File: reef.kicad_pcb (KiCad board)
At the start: 2 copper layers, 60 parts, among them J1 T4140012051-000, J2 T4140012051-000, U1 nice_nano

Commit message: PCB Layout
layout of keys, controller board, connectors + routed matrix columns
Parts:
- added MX1: MX-NoLED, MX_Only:MXOnly-1U-Hotswap, B.Cu at (46.8, 62.7)
- added MX10: MX-NoLED, MX_Only:MXOnly-1U-Hotswap, B.Cu at (84.9, 75.4)
- added MX11: MX-NoLED, MX_Only:MXOnly-1U-Hotswap, B.Cu at (84.9, 94.5)
- added MX12: MX-NoLED, MX_Only:MXOnly-1U-Hotswap, B.Cu at (84.9, 113.5)
- added MX13: MX-NoLED, MX_Only:MXOnly-1U-Hotswap, B.Cu at (104.0, 59.5)
- added MX14: MX-NoLED, MX_Only:MXOnly-1U-Hotswap, B.Cu at (104.0, 78.6)
- added MX15: MX-NoLED, MX_Only:MXOnly-1U-Hotswap, B.Cu at (104.0, 97.6)
- added MX16: MX-NoLED, MX_Only:MXOnly-1U-Hotswap, B.Cu at (104.0, 116.7)
- added MX17: MX-NoLED, MX_Only:MXOnly-1U-Hotswap, B.Cu at (123.0, 62.7)
- added MX18: MX-NoLED, MX_Only:MXOnly-1U-Hotswap, B.Cu at (123.0, 81.8)
- added MX19: MX-NoLED, MX_Only:MXOnly-1U-Hotswap, B.Cu at (123.0, 100.8)
- added MX2: MX-NoLED, MX_Only:MXOnly-1U-Hotswap, B.Cu at (46.8, 81.8)
- added MX20: MX-NoLED, MX_Only:MXOnly-1U-Hotswap, B.Cu at (123.0, 119.9)
- added MX21: MX-NoLED, MX_Only:MXOnly-1U-Hotswap, B.Cu at (142.1, 65.9)
- added MX22: MX-NoLED, MX_Only:MXOnly-1U-Hotswap, B.Cu at (142.1, 84.9)
- added MX23: MX-NoLED, MX_Only:MXOnly-1U-Hotswap, B.Cu at (142.1, 104.0)
- added MX24: MX-NoLED, MX_Only:MXOnly-1U-Hotswap, B.Cu at (217.5, 79.4)
- added MX25: MX-NoLED, MX_Only:MXOnly-2U-Hotswap, B.Cu at (217.5, 108.0)
- added MX26: MX-NoLED, MX_Only:MXOnly-1.25U-Hotswap, B.Cu at (238.9, 79.4)
- added MX27: MX-NoLED, MX_Only:MXOnly-1.25U-Hotswap, B.Cu at (238.9, 98.4)
- added MX28: MX-NoLED, MX_Only:MXOnly-1.25U-Hotswap, B.Cu at (238.9, 117.5)
- added MX3: MX-NoLED, MX_Only:MXOnly-1U-Hotswap, B.Cu at (46.8, 100.8)
- added MX4: MX-NoLED, MX_Only:MXOnly-1U-Hotswap, B.Cu at (46.8, 119.9)
- added MX5: MX-NoLED, MX_Only:MXOnly-1U-Hotswap, B.Cu at (65.9, 59.5)
- added MX6: MX-NoLED, MX_Only:MXOnly-1U-Hotswap, B.Cu at (65.9, 78.6)
- added MX7: MX-NoLED, MX_Only:MXOnly-1U-Hotswap, B.Cu at (65.9, 97.6)
- added MX8: MX-NoLED, MX_Only:MXOnly-1U-Hotswap, B.Cu at (65.9, 116.7)
- added MX9: MX-NoLED, MX_Only:MXOnly-1U-Hotswap, B.Cu at (84.9, 56.4)
- moved D26 231.1 mm to (260.4, 94.5)
- moved MX27 206.6 mm to (238.9, 98.4)
- moved D28 201.1 mm to (260.4, 107.2)
- moved MX25 193.4 mm to (217.5, 108.0), turned to 90 degrees
- moved D27 184.5 mm to (260.4, 100.8)
- moved MX28 182.2 mm to (238.9, 117.5)
- moved MX26 173.1 mm to (238.9, 79.4)
- moved D10 151.7 mm to (139.3, 164.5)
- moved D12 151.7 mm to (150.8, 161.1)
- moved D15 151.7 mm to (145.1, 161.1)
- moved D16 151.7 mm to (139.3, 171.2)
- moved D19 151.7 mm to (145.1, 164.5)
- moved D21 151.7 mm to (139.3, 161.1)
- moved D6 151.7 mm to (139.3, 167.8)
- moved J1 135.2 mm to (164.3, 70.8)
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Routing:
- net col_2: track 0.00 -> 143.6 mm, vias 0 -> 4
- net col_0: track 0.00 -> 143.6 mm, vias 0 -> 4
- net col_4: track 0.00 -> 143.6 mm, vias 0 -> 4
- net col_3: track 0.00 -> 143.6 mm, vias 0 -> 4
- net col_1: track 0.00 -> 143.6 mm, vias 0 -> 4
- net thc_7: track 0.00 -> 130.9 mm, vias 0 -> 3
- net thc_6: track 0.00 -> 111.9 mm, vias 0 -> 2
- net col_5: track 0.00 -> 102.9 mm, vias 0 -> 3

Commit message: PCB updates + importing keebio library
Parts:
- D1, D10, D11, D12, D13, D14, D15, D16, D17, D18, D19, D2, D20, D21, D22, D23, D24, D25, D26, D27, D28, D29, D3, D4, D5, D6, D7, D8, D9: footprint Diode_SMD:D_SOD-123 -> modified_footprints:D_SOD-123_reversible
- moved D24 43.0 mm to (217.5, 85.7)
- moved D25 40.5 mm to (224.6, 108.0), turned to 90 degrees
- moved D28 27.2 mm to (238.9, 123.8)
- moved D26 23.1 mm to (238.9, 85.7)
- moved D27 21.8 mm to (238.9, 104.8)

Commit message: Updated Layout
modified layout to use trrs to connect with thumb cluster, added connector for battery, and footprint for nice!view display
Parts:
- removed D29: D_Small, modified_footprints:D_SOD-123_reversible
- removed the MX24 at (217.5, 79.4) (x2)
- removed the MX25 at (217.5, 108.0) (x2)
- removed the MX26 at (238.9, 79.4) (x2)
- removed the MX27 at (238.9, 98.4) (x2)
- removed the MX28 at (238.9, 117.5) (x2)
- added MX24: MX-NoLED, MX_Only:MXOnly-1U-Hotswap, F.Cu at (142.1, 123.0)
- added MX25: MX-NoLED, MX_Only:MXOnly-2.25U-Hotswap, F.Cu at (337.3, 116.7)
- added MX26: MX-NoLED, MX_Only:MXOnly-1.5U-Hotswap, F.Cu at (361.2, 90.5)
- added MX27: MX-NoLED, MX_Only:MXOnly-1.5U-Hotswap, F.Cu at (361.2, 109.5)
- added MX28: MX-NoLED, MX_Only:MXOnly-1.5U-Hotswap, F.Cu at (361.2, 128.6)
- added U2: TRRS, Keebio-Parts:TRRS-PJ-320A, F.Cu at (166.7, 39.3)
- added U3: TRRS, Keebio-Parts:TRRS-PJ-320A, F.Cu at (329.8, 84.0)
- J1: value T4140012051-000 -> Conn_01x05_Female; footprint footprints:CONN5_T4140012051_TEC -> modified_footprints:nice_view_adapted
- J2: value T4140012051-000 -> Conn_01x02_Male; footprint footprints:CONN5_T4140012051_TEC -> Connector_JST:JST_PH_S2B-PH-K_1x02_P2.00mm_Horizontal
- moved D14 106.9 mm to (104.0, 84.9)
- moved D6 106.1 mm to (65.9, 91.3)
- moved D9 105.5 mm to (84.9, 69.1)
- moved D26 102.4 mm to (161.9, 153.2)
- moved D23 101.8 mm to (142.1, 110.3)
- moved D13 100.8 mm to (104.0, 65.9)
- moved D17 95.0 mm to (123.0, 69.1)
- moved D3 93.9 mm to (46.8, 113.5)
- moved D10 93.8 mm to (84.9, 88.1)
- moved D5 93.7 mm to (65.9, 72.2)
- moved D21 88.9 mm to (142.1, 72.2)
- moved D24 87.1 mm to (142.1, 129.4)
- moved D18 86.4 mm to (123.0, 88.1)
- moved D1 84.8 mm to (46.8, 75.4)
- moved D22 78.8 mm to (142.1, 91.3)
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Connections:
- D24 pad 1: thr_0 -> row_3
- D25 pad 1: thr_1 -> thr_0
- D28 pad 1: thr_2 -> thr_1
- J1 pad 1: row_2 -> mosi
- J1 pad 2: row_1 -> sck
- J1 pad 3: row_0 -> vcc
- J1 pad 4: col_6 -> gnd
- J1 pad 5: col_7 -> cs
- J2 pad 1: thr_2 -> bat+
- J2 pad 2: thr_1 -> gnd
- U1 pad 1: unconnected-(U1-Pad1) -> cs
- U1 pad 21: unconnected-(U1-Pad21) -> vcc
- U1 pad 23: unconnected-(U1-Pad23) -> gnd
- U1 pad 24: unconnected-(U1-Pad24) -> bat+
- U1 pad 3: unconnected-(U1-Pad3) -> gnd
- U1 pad 4: unconnected-(U1-Pad4) -> gnd
- U1 pad 5: unconnected-(U1-Pad5) -> mosi
- U1 pad 6: unconnected-(U1-Pad6) -> sck
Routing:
- net thc_7: track 130.9 -> 2.82 mm, vias 3 -> 0
- net thc_6: track 111.9 -> 6.38 mm, vias 2 -> 0
- net bat+: track 0.00 -> 9.48 mm
- net row_1: track 0.00 -> 6.82 mm
- net row_0: track 0.00 -> 6.63 mm
- net col_6: track 0.00 -> 6.63 mm
- net thr_1: track 0.00 -> 6.56 mm
- net thr_0: track 0.00 -> 6.38 mm
- net col_7: track 0.00 -> 2.57 mm
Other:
- board text added: "J2"

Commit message: Flipside Linkage
connected diode pads to their flipside counterparts, thumb cluster should now be fully routed, to be ground-planed later
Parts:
- D26: moved to B.Cu
- moved U3 108.4 mm to (221.9, 93.6)
- moved MX26 108.3 mm to (253.2, 99.2)
- moved MX27 108.3 mm to (253.2, 118.3)
- moved MX25 108.3 mm to (229.4, 125.4)
- moved MX28 108.3 mm to (253.2, 137.3)
- moved D26 102.9 mm to (253.2, 105.6), turned to 180 degrees
- moved D28 86.0 mm to (253.2, 143.7)
- moved D27 79.3 mm to (253.2, 124.6)
- moved D25 57.9 mm to (235.7, 125.4), turned to 90 degrees
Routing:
- net thc_6: track 6.38 -> 91.3 mm, vias 0 -> 2
- net thc_7: track 2.82 -> 78.5 mm, vias 0 -> 2
- net thr_0: track 6.38 -> 69.8 mm, vias 0 -> 2
- net thr_1: track 6.56 -> 57.3 mm, vias 0 -> 2
- net row_3: track 0.00 -> 23.7 mm, vias 0 -> 6
- net row_1: track 6.82 -> 30.6 mm, vias 0 -> 6
- net row_2: track 0.00 -> 23.7 mm, vias 0 -> 6
- net row_0: track 6.63 -> 30.4 mm, vias 0 -> 6
- net mosi: track 0.00 -> 16.0 mm
- net sck: track 0.00 -> 15.0 mm
- net cs: track 0.00 -> 13.1 mm
- net gnd: track 0.00 -> 5.81 mm
- net Net-(D8-Pad2): track 0.00 -> 3.96 mm, vias 0 -> 1
- net Net-(D28-Pad2): track 0.00 -> 3.96 mm, vias 0 -> 1
- net Net-(D20-Pad2): track 0.00 -> 3.96 mm, vias 0 -> 1
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
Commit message: Thumb Cluster Routing
thumb cluster routing should NOW be complete (rows were not connected up previously)
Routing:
- net thr_1: track 57.3 -> 76.7 mm
- net Net-(D28-Pad2): track 3.96 -> 20.5 mm
- net Net-(D25-Pad2): track 3.30 -> 18.9 mm
- net Net-(D26-Pad2): track 3.96 -> 18.8 mm
- net Net-(D27-Pad2): track 3.89 -> 18.1 mm
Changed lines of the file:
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@@
   (segment (start 235.74375 123.7625) (end 235.74375 122.2375) (width 0.25) (layer "B.Cu") (net 28))
   (segment (start 235.74375 122.2375) (end 234.15625 120.65) (width 0.25) (layer "B.Cu") (net 28))
+  (segment (start 253.20625 125.4125) (end 253.20625 133.969296) (width 0.25) (layer "F.Cu") (net 29))
+  (segment (start 250.825 136.350546) (end 250.825 140.49375) (width 0.25) (layer "F.Cu") (net 29))
+  (segment (start 250.825 140.49375) (end 253.20625 142.875) (width 0.25) (layer "F.Cu") (net 29))
   (segment (start 253.20625 142.875) (end 252.35 142.875) (width 0.25) (layer "F.Cu") (net 29))
+  (segment (start 253.20625 133.969296) (end 250.825 136.350546) (width 0.25) (layer "F.Cu") (net 29))
   (segment (start 252.35 125.4125) (end 251.55625 124.61875) (width 0.25) (layer "F.Cu") (net 29))
   (segment (start 253.20625 125.4125) (end 252.35 125.4125) (width 0.25) (layer "F.Cu") (net 29))
@@
   (via (at 235.74375 125.4125) (size 0.8) (drill 0.4) (layers "F.Cu" "B.Cu") (net 30))
   (segment (start 235.74375 127.0625) (end 235.74375 125.4125) (width 0.25) (layer "B.Cu") (net 30))
+  (segment (start 231.795479 119.082979) (end 233.3625 120.65) (width 0.25) (layer "B.Cu") (net 30))
+  (segment (start 224.801271 119.082979) (end 231.795479 119.082979) (width 0.25) (layer "B.Cu") (net 30))
+  (segment (start 233.3625 123.03125) (end 235.74375 125.4125) (width 0.25) (layer "B.Cu") (net 30))
+  (segment (start 224.31375 119.5705) (end 224.801271 119.082979) (width 0.25) (layer "B.Cu") (net 30))
+  (segment (start 233.3625 120.65) (end 233.3625 123.03125) (width 0.25) (layer "B.Cu") (net 30))
+  (segment (start 246.876729 94.626271) (end 246.876729 100.826729) (width 0.25) (layer "F.Cu") (net 31))
+  (segment (start 247.36425 94.13875) (end 246.876729 94.626271) (width 0.25) (layer "F.Cu") (net 31))
   (segment (start 254.85625 105.56875) (end 254 105.56875) (width 0.25) (layer "F.Cu") (net 31))
+  (segment (start 249.2375 103.1875) (end 251.61875 103.1875) (width 0.25) (layer "F.Cu") (net 31))
+  (segment (start 246.876729 100.826729) (end 249.2375 103.1875) (width 0.25) (layer "F.Cu") (net 31))
+  (segment (start 251.61875 103.1875) (end 253.20625 104.775) (width 0.25) (layer "F.Cu") (net 31))
   (segment (start 254 105.56875) (end 253.20625 104.775) (width 0.25) (layer "F.Cu") (net 31))
   (via (at 253.20625 104.775) (size 0.8) (drill 0.4) (layers "F.Cu" "B.Cu") (net 31))
   (segment (start 252.35 104.775) (end 251.55625 105.56875) (width 0.25) (layer "B.Cu") (net 31))
   (segment (start 253.20625 104.775) (end 252.35 104.775) (width 0.25) (layer "B.Cu") (net 31))
+  (segment (start 247.36425 113.18875) (end 246.876729 113.676271) (width 0.25) (layer "F.Cu") (net 32))
   (segment (start 254.85625 124.61875) (end 253.831652 124.61875) (width 0.25) (layer "F.Cu") (net 32))
+  (segment (start 246.876729 113.676271) (end 246.876729 118.78632) (width 0.25) (layer "F.Cu") (net 32))
+  (segment (start 251.121659 123.03125) (end 252.244152 123.03125) (width 0.25) (layer "F.Cu") (net 32))
   (segment (start 253.831652 124.61875) (end 253.122076 123.909174) (width 0.25) (layer "F.Cu") (net 32))
+  (segment (start 252.244152 123.03125) (end 253.122076 123.909174) (width 0.25) (layer "F.Cu") (net 32))
+  (segment (start 246.876729 118.78632) (end 251.121659 123.03125) (width 0.25) (layer "F.Cu") (net 32))
   (via (at 253.122076 123.909174) (size 0.8) (drill 0.4) (layers "F.Cu" "B.Cu") (net 32))
   (segment (start 253.122076 123.909174) (end 252.265826 123.909174) (width 0.25) (layer "B.Cu") (net 32))
   (segment (start 252.265826 123.909174) (end 251.55625 124.61875) (width 0.25) (layer "B.Cu") (net 32))
+  (segment (start 246.876729 132.726271) (end 246.876729 140.514229) (width 0.25) (layer "F.Cu") (net 33))
+  (segment (start 253.075489 144.593261) (end 253.20625 144.4625) (width 0.25) (layer "F.Cu") (net 33))
+  (segment (start 246.876729 140.514229) (end 250.955761 144.593261) (width 0.25) (layer "F.Cu") (net 33))
+  (segment (start 250.955761 144.593261) (end 253.075489 144.593261) (width 0.25) (layer "F.Cu") (net 33))
   (segment (start 254.85625 143.66875) (end 254 143.66875) (width 0.25) (layer "F.Cu") (net 33))
   (segment (start 254 143.66875) (end 253.20625 144.4625) (width 0.25) (layer "F.Cu") (net 33))
+  (segment (start 247.36425 132.23875) (end 246.876729 132.726271) (width 0.25) (layer "F.Cu") (net 33))
   (via (at 253.20625 144.4625) (size 0.8) (drill 0.4) (layers "F.Cu" "B.Cu") (net 33))
   (segment (start 252.35 144.4625) (end 251.55625 143.66875) (width 0.25) (layer "B.Cu") (net 33))

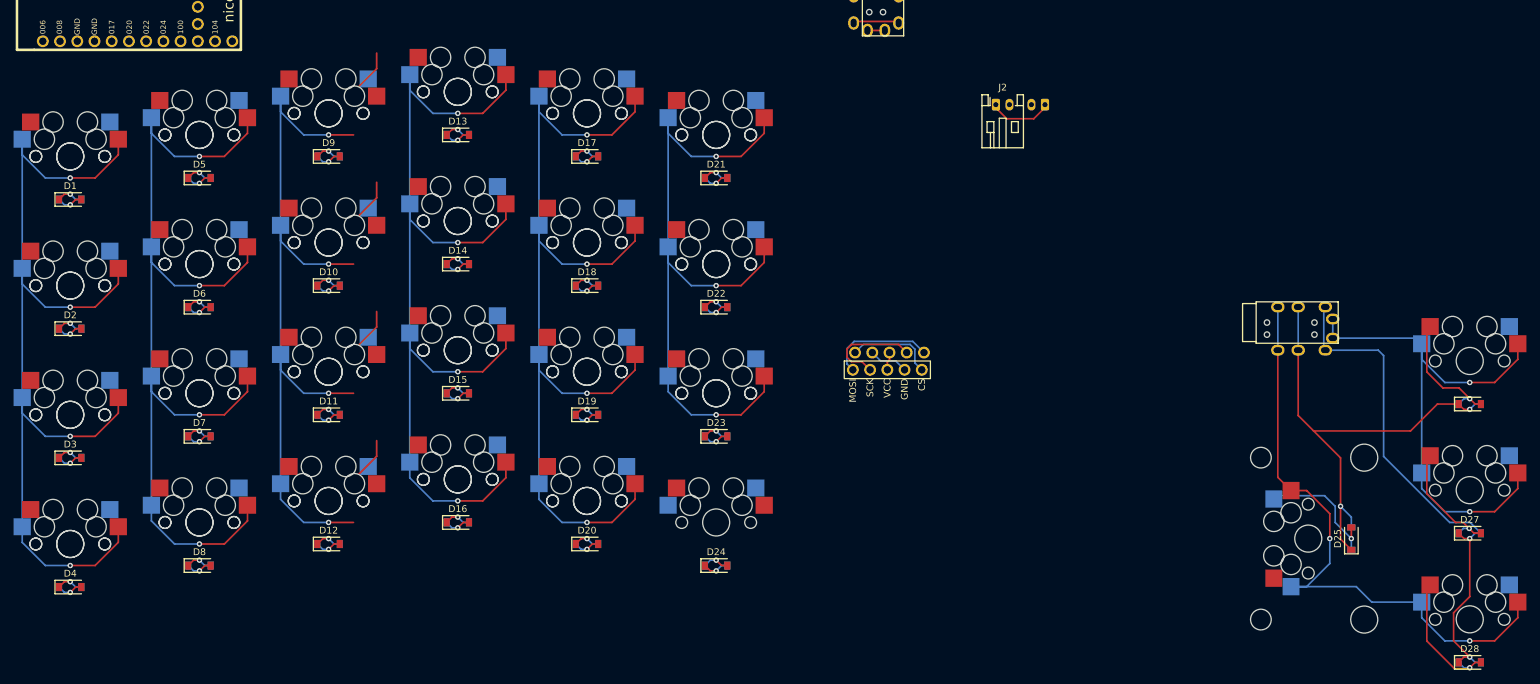
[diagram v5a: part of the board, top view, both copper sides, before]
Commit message: Matrix Routing
Routing for the switch matrix (including some things missed from the thumb cluster yet again) should now be complete
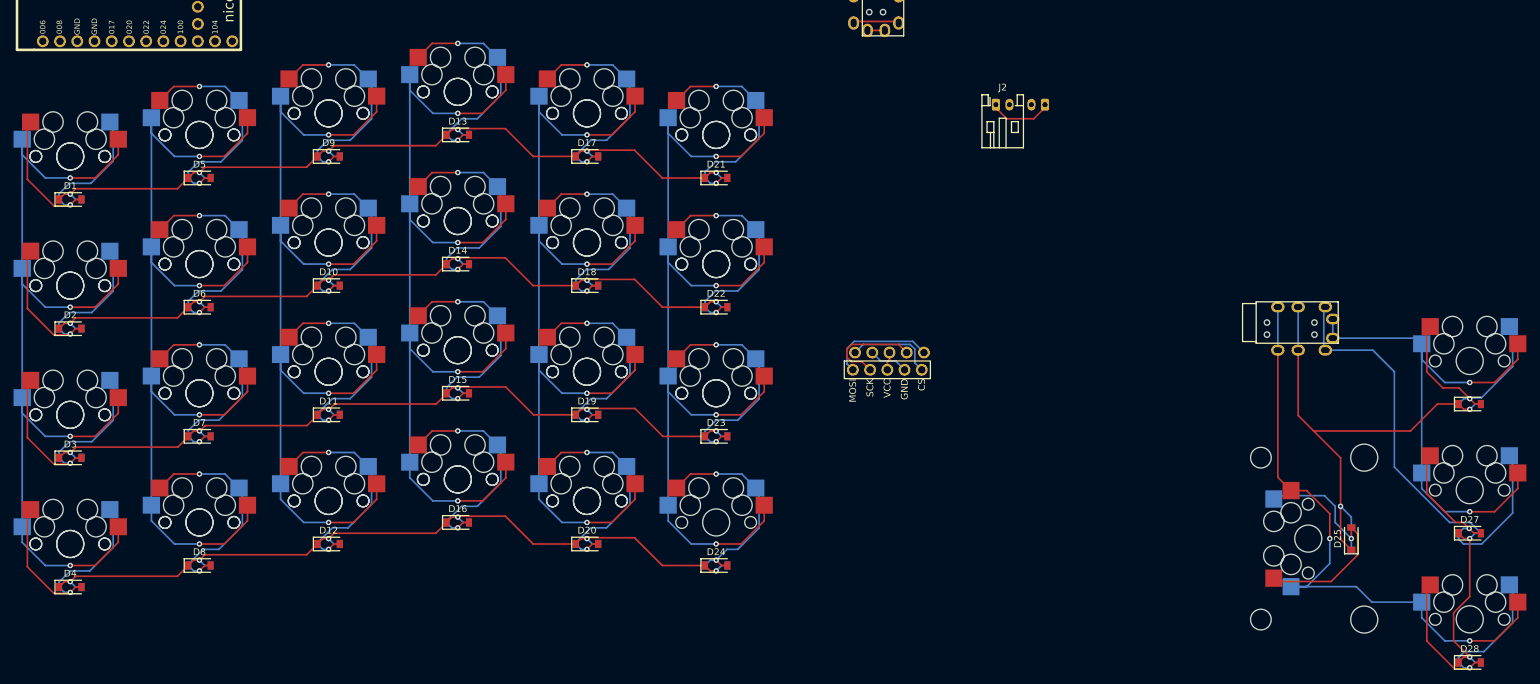
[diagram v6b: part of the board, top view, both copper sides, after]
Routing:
- net row_2: track 23.7 -> 117.2 mm
- net row_0: track 30.4 -> 123.8 mm
- net row_1: track 30.6 -> 124.0 mm
- net row_3: track 23.7 -> 117.2 mm
- net col_5: track 102.9 -> 143.6 mm, vias 3 -> 4
- net Net-(D3-Pad2): track 3.96 -> 37.5 mm
- net Net-(D2-Pad2): track 3.96 -> 37.5 mm
- net Net-(D1-Pad2): track 3.96 -> 37.4 mm
- net Net-(D4-Pad2): track 3.96 -> 37.2 mm
- net Net-(D9-Pad2): track 3.96 -> 34.2 mm, vias 1 -> 2
- net Net-(D22-Pad2): track 3.96 -> 34.2 mm, vias 1 -> 2
- net Net-(D18-Pad2): track 3.96 -> 34.2 mm, vias 1 -> 2
- net Net-(D15-Pad2): track 3.96 -> 34.2 mm, vias 1 -> 2
- net Net-(D14-Pad2): track 3.96 -> 34.2 mm, vias 1 -> 2
- net Net-(D5-Pad2): track 3.96 -> 34.2 mm, vias 1 -> 2
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
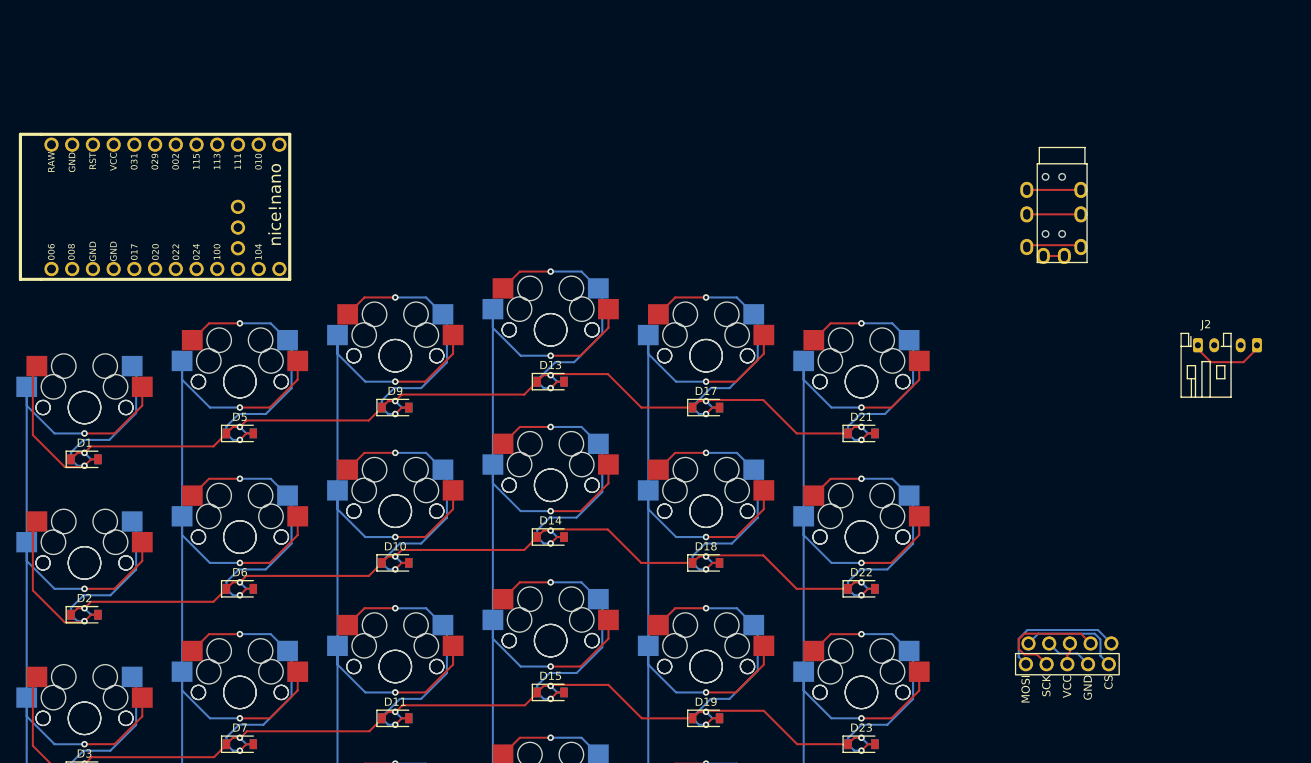
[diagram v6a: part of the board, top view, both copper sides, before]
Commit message: Route Display
Display connected to nice!nano. in order to keep pcb reversible, jumper wire will be soldered between the actual display pad footprint and the appropriate column of pads (J1)
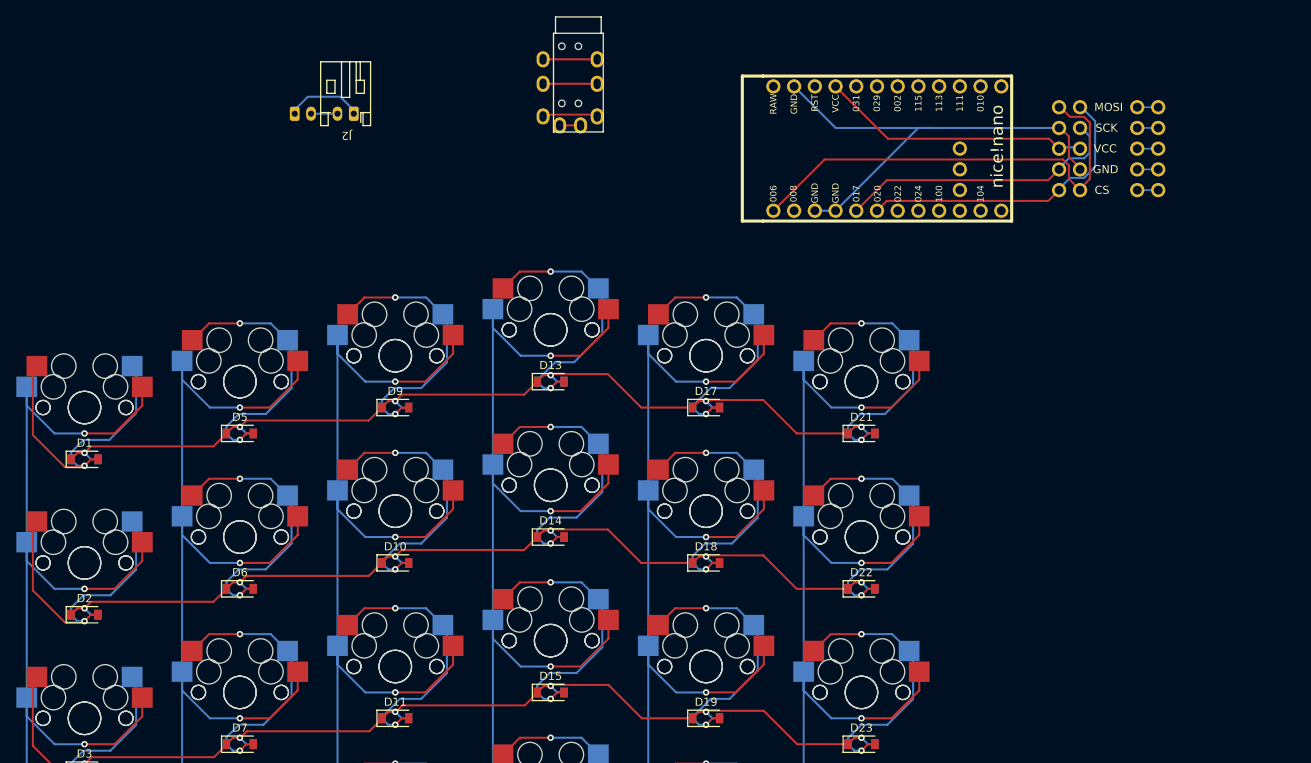
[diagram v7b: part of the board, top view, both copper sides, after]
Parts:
- added Display1: nice!view, modified_footprints:nice_view_adapted, B.Cu at (192.9, 37.4)
- J1, J2: moved to B.Cu
- moved J2 115.9 mm to (73.5, 30.1)
- moved U1 88.8 mm to (145.3, 37.3)
- moved U2 61.4 mm to (107.4, 23.3)
- moved J1 46.7 mm to (167.6, 37.3), turned to 90 degrees
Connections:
- U1 pad 5: mosi -> sck
- U1 pad 6: sck -> mosi
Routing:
- net gnd: track 5.81 -> 62.8 mm
- net cs: track 13.1 -> 56.0 mm
- net vcc: track 2.67 -> 33.1 mm
- net mosi: track 16.0 -> 37.1 mm
- net sck: track 15.0 -> 35.2 mm
- net (no net): track 0.00 -> 12.8 mm
